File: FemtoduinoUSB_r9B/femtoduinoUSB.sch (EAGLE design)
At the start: 29 parts, among them IC1 ATMEGA168MLF, IC2 FT231XQ-R, U1 MIC5205

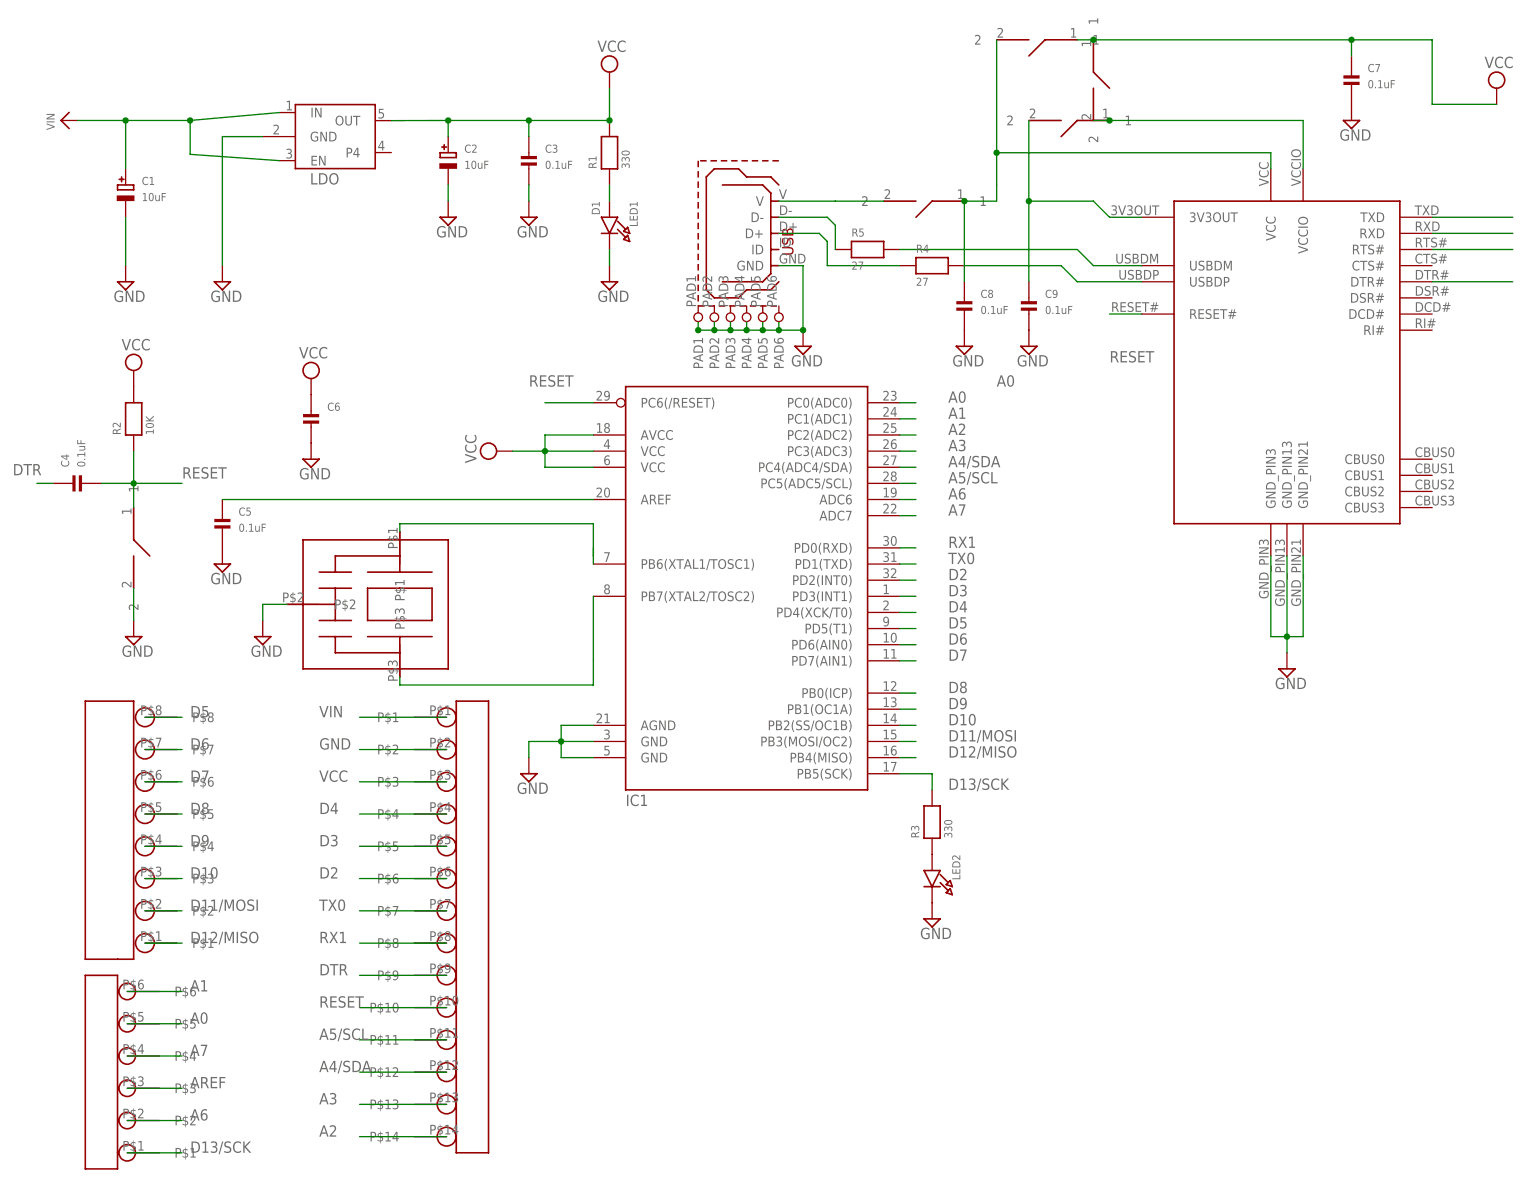
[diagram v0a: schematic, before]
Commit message: Committing revision 9B of the FemtoduinoUSB. Minor corrections to the schematic, as the FTDI chip RESET# line was erroneously connected, instead of RST, to the ATMEGA DTR line. Additionally, a wire in the schematic was not connected, even though it appeared to be for some reason. It has been connected, and the board file updated.'
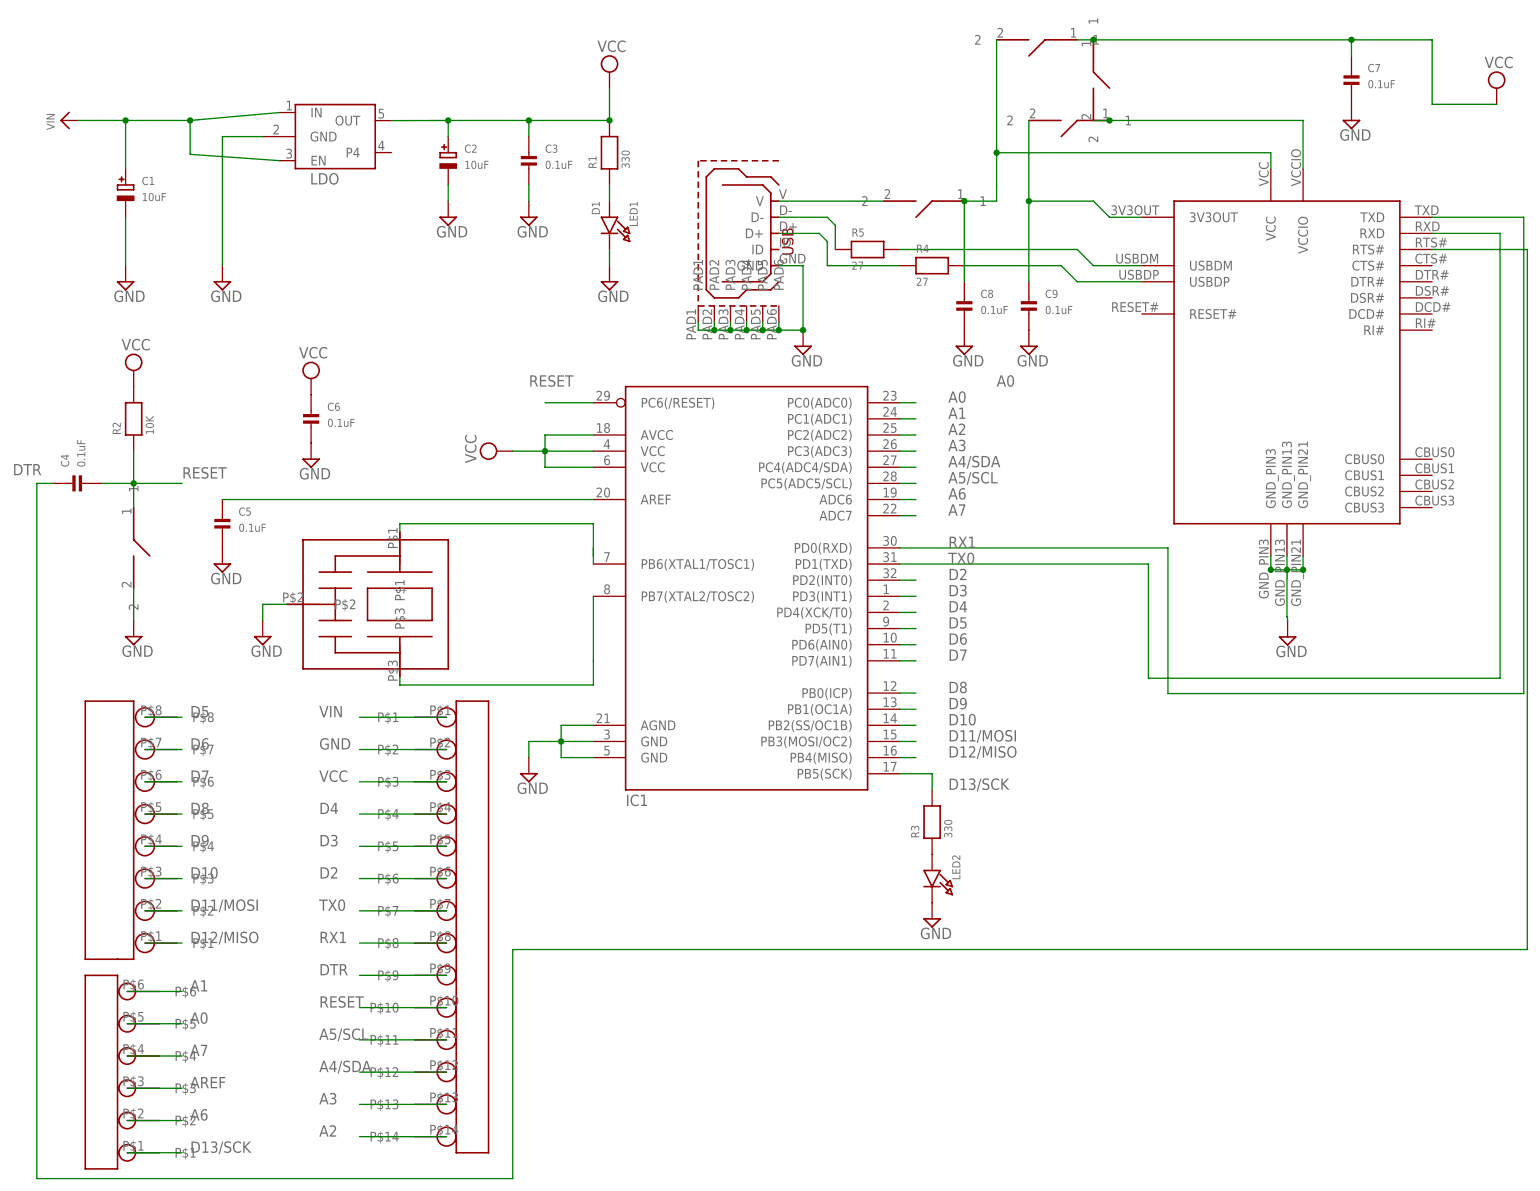
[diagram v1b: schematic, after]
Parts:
- C6: value (none) -> 0.1uF
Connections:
- removed net N$3: IC2.RTS#
- net DTR: now also IC2.RTS#
- net GND: now also USB1.PAD1, USB1.PAD2, USB1.PAD3, USB1.PAD4, USB1.PAD5, USB1.PAD6
- net RESET: no longer IC2.DTR#, IC2.RESET#
